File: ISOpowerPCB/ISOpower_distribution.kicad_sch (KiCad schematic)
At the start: 27 parts, among them M1 Fan_IEC60617, Q2 IRF5305_PBF, Q3 IRF5305_PBF, U10 LM2596S-5, U4 i6A4W020A-DC-DC-250W, U5 i6A4W020A-DC-DC-250W, U6 ACS712xLCTR-30A, U7 ACS712xLCTR-30A

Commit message: Footprint Associations 50% complete
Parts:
- C10, C20, C21, C9: footprint Capacitor_SMD:CP_Elec_10x10 -> Capacitor_SMD:CP_Elec_6.3x7.7
- C13, C14: footprint Capacitor_SMD:CP_Elec_6.3x5.9 -> Capacitor_SMD:CP_Elec_6.3x5.4
- C19: footprint Capacitor_SMD:CP_Elec_10x10 -> Capacitor_THT:C_Radial_D12.5mm_H20.0mm_P5.00mm
- D3: footprint Diode_THT:D_DO-201AD_P15.24mm_Horizontal -> Diode_SMD:D_SMA
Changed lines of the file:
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@@
     (property "Reference" "D3" (id 0) (at 247.65 140.97 90))
     (property "Value" "1N5821" (id 1) (at 246.38 144.78 90))
-    (property "Footprint" "Diode_THT:D_DO-201AD_P15.24mm_Horizontal" (id 2) (at 241.935 138.43 0)
+    (property "Footprint" "Diode_SMD:D_SMA" (id 2) (at 241.935 138.43 0)
       (effects (font (size 1.27 1.27)) hide)
     )
@@
       (effects (font (size 1.27 1.27)) (justify left))
     )
-    (property "Footprint" "Capacitor_SMD:CP_Elec_10x10" (id 2) (at 260.0452 142.24 0)
+    (property "Footprint" "Capacitor_SMD:CP_Elec_6.3x7.7" (id 2) (at 260.0452 142.24 0)
       (effects (font (size 1.27 1.27)) hide)
     )
@@
       (effects (font (size 1.27 1.27)) (justify left))
     )
-    (property "Footprint" "Capacitor_SMD:CP_Elec_10x10" (id 2) (at 206.7052 139.7 0)
+    (property "Footprint" "Capacitor_THT:C_Radial_D12.5mm_H20.0mm_P5.00mm" (id 2) (at 206.7052 139.7 0)
       (effects (font (size 1.27 1.27)) hide)
     )
@@
       (effects (font (size 1.27 1.27)) (justify left))
     )
-    (property "Footprint" "Capacitor_SMD:CP_Elec_6.3x5.9" (id 2) (at 122.8852 158.75 0)
+    (property "Footprint" "Capacitor_SMD:CP_Elec_6.3x5.4" (id 2) (at 122.8852 158.75 0)
       (effects (font (size 1.27 1.27)) hide)
     )
@@
       (effects (font (size 1.27 1.27)) (justify left))
     )
-    (property "Footprint" "Capacitor_SMD:CP_Elec_10x10" (id 2) (at 229.5652 63.5 0)
+    (property "Footprint" "Capacitor_SMD:CP_Elec_6.3x7.7" (id 2) (at 229.5652 63.5 0)
       (effects (font (size 1.27 1.27)) hide)
     )
@@
       (effects (font (size 1.27 1.27)) (justify left))
     )
-    (property "Footprint" "Capacitor_SMD:CP_Elec_10x10" (id 2) (at 41.6052 77.47 0)
+    (property "Footprint" "Capacitor_SMD:CP_Elec_6.3x7.7" (id 2) (at 41.6052 77.47 0)
       (effects (font (size 1.27 1.27)) hide)
     )
@@
       (effects (font (size 1.27 1.27)) (justify left))
     )
-    (property "Footprint" "Capacitor_SMD:CP_Elec_6.3x5.9" (id 2) (at 126.6952 80.01 0)
+    (property "Footprint" "Capacitor_SMD:CP_Elec_6.3x5.4" (id 2) (at 126.6952 80.01 0)
       (effects (font (size 1.27 1.27)) hide)
     )
@@
       (effects (font (size 1.27 1.27)) (justify left))
     )
-    (property "Footprint" "Capacitor_SMD:CP_Elec_10x10" (id 2) (at 42.8752 153.67 0)
-      (effects (font (size 1.27 1.27)) hide)
-    )
+    (property "Footprint" "Capacitor_SMD:CP_Elec_6.3x7.7" (id 2) (at 42.8752 153.67 0)
+      (effects (font (size 1.27 1.27)) hide)
+    )

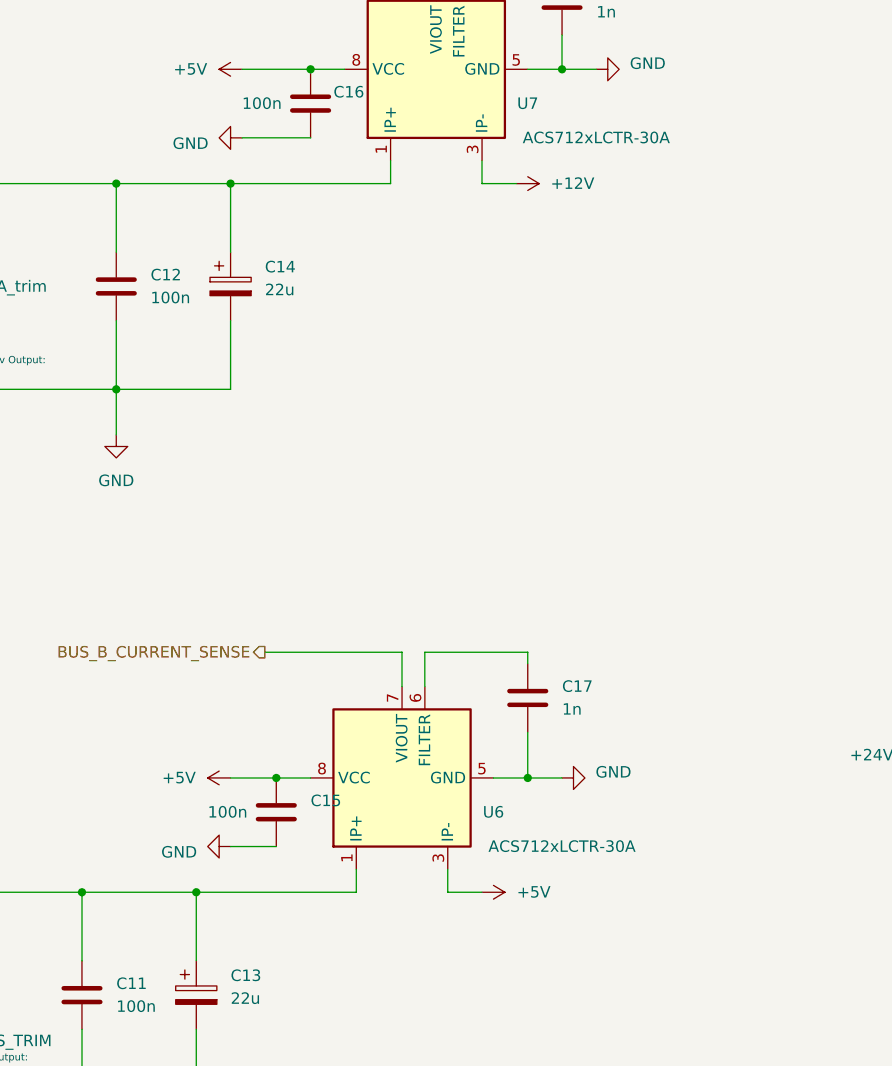
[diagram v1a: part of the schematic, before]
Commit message: added documentation for component selection
Completed footprint association & added documentation re Netclasses. Need to update netclasses in schematic settings before moving to PCB layout.
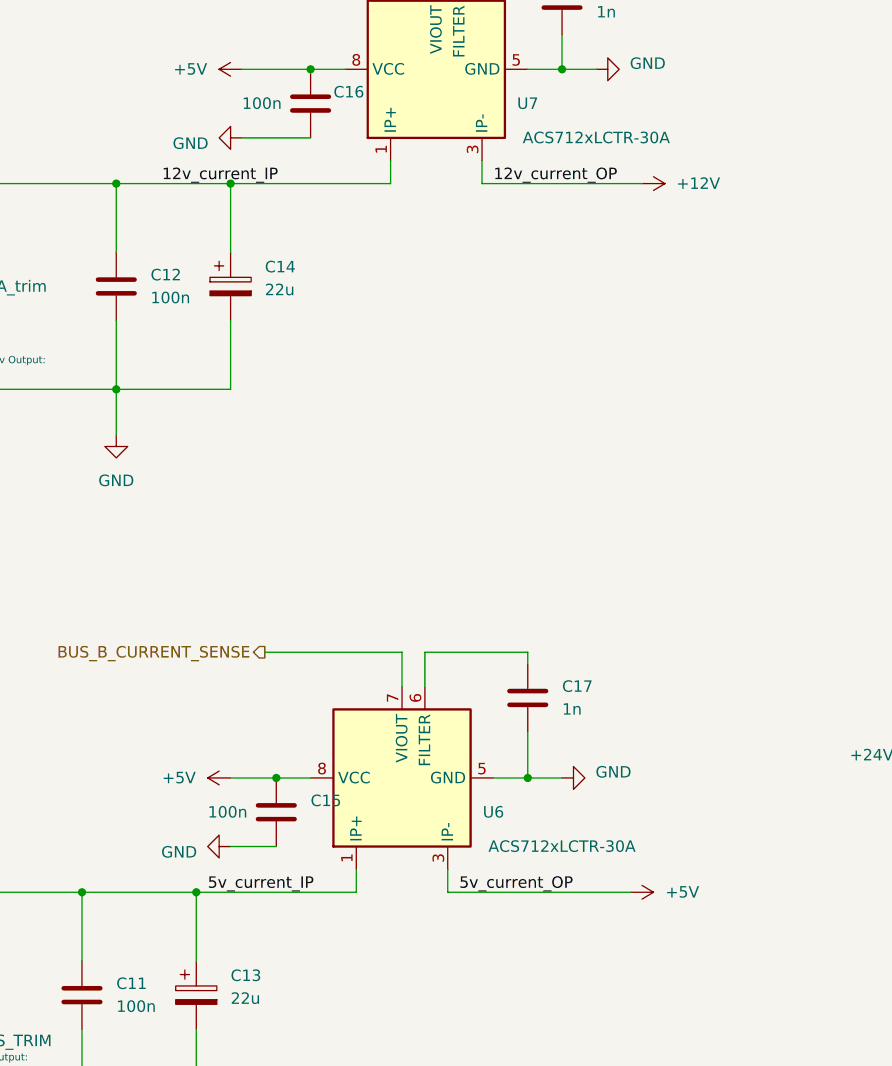
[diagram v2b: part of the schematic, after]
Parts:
- JP2, JP3: footprint (none) -> Jumper:SolderJumper-2_P1.3mm_Open_RoundedPad1.0x1.5mm
- L2: footprint (none) -> Inductor_SMD:L_12x12mm_H8mm
- M1: footprint Fuse:Fuseholder_Keystone_3555-2 -> ISOpower:Fan12V_40by10.5mm
- Q2, Q3: footprint Package_TO_SOT_THT:TO-220-3_Vertical -> Package_TO_SOT_SMD:TO-263-2
- R6, R7: footprint Resistor_SMD:R_0805_2012Metric_Pad1.20x1.40mm_HandSolder -> Resistor_THT:R_Axial_DIN0309_L9.0mm_D3.2mm_P12.70mm_Horizontal
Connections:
- net 5v_current_IP: now reaches C11.1, C13.1, U4.7 (Sense(+)), U4.8 (Vout(+)), U6.1 (IP+), U6.2 (IP+)
- net 12v_current_IP: now reaches C12.1, C14.1, U5.7 (Sense(+)), U5.8 (Vout(+)), U7.1 (IP+), U7.2 (IP+)
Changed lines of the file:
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@@
     (stroke (width 0) (type default) (color 0 0 0 0))
   )
-  (wire (pts (xy 149.86 143.51) (xy 153.67 143.51))
+  (wire (pts (xy 149.86 143.51) (xy 170.18 143.51))
     (stroke (width 0) (type default) (color 0 0 0 0))
   )
@@
     (stroke (width 0) (type default) (color 0 0 0 0))
   )
-  (wire (pts (xy 153.67 64.77) (xy 157.48 64.77))
+  (wire (pts (xy 153.67 64.77) (xy 171.45 64.77))
     (stroke (width 0) (type default) (color 0 0 0 0))
   )
@@
     (effects (font (size 1.27 1.27)) (justify left bottom))
   )
+  (label "12v_current_IP" (at 118.11 64.77 0)
+    (effects (font (size 1.27 1.27)) (justify left bottom))
+  )
+  (label "5v_current_OP" (at 151.13 143.51 0)
+    (effects (font (size 1.27 1.27)) (justify left bottom))
+  )
+  (label "12v_current_OP" (at 154.94 64.77 0)
+    (effects (font (size 1.27 1.27)) (justify left bottom))
+  )
   (label "12V_BUS" (at 29.21 30.48 0)
     (effects (font (size 1.27 1.27)) (justify left bottom))
@@
   )
   (label "MCU_5V" (at 260.35 133.35 0)
+    (effects (font (size 1.27 1.27)) (justify left bottom))
+  )
+  (label "5v_current_IP" (at 123.19 143.51 0)
     (effects (font (size 1.27 1.27)) (justify left bottom))
   )
@@
     (pin "1")
   )
-  (symbol (lib_id "power:+5V") (at 153.67 143.51 270) (unit 1)
-    (in_bom yes) (on_board yes)
-    (property "Reference" "#PWR043" (id 0) (at 149.86 143.51 0)
-      (effects (font (size 1.27 1.27)) hide)
-    )
-    (property "Value" "+5V" (id 1) (at 161.29 143.51 90)
+  (symbol (lib_id "power:+5V") (at 170.18 143.51 270) (unit 1)
+    (in_bom yes) (on_board yes)
+    (property "Reference" "#PWR043" (id 0) (at 166.37 143.51 0)
+      (effects (font (size 1.27 1.27)) hide)
+    )
+    (property "Value" "+5V" (id 1) (at 177.8 143.51 90)
       (effects (font (size 1.27 1.27)) (justify right))
     )
-    (property "Footprint" "" (id 2) (at 153.67 143.51 0)
-      (effects (font (size 1.27 1.27)) hide)
-    )
-    (property "Datasheet" "" (id 3) (at 153.67 143.51 0)
+    (property "Footprint" "" (id 2) (at 170.18 143.51 0)
+      (effects (font (size 1.27 1.27)) hide)
+    )
+    (property "Datasheet" "" (id 3) (at 170.18 143.51 0)
       (effects (font (size 1.27 1.27)) hide)
     )
@@
     (property "Reference" "L2" (id 0) (at 251.46 130.81 90))
     (property "Value" "33uH" (id 1) (at 252.73 134.62 90))
-    (property "Footprint" "" (id 2) (at 252.73 133.35 0)
+    (property "Footprint" "Inductor_SMD:L_12x12mm_H8mm" (id 2) (at 252.73 133.35 0)
       (effects (font (size 1.27 1.27)) hide)
     )
@@
       (effects (font (size 1.27 1.27)) (justify left))
     )
-    (property "Footprint" "Resistor_SMD:R_0805_2012Metric_Pad1.20x1.40mm_HandSolder" (id 2) (at 93.472 82.55 90)
+    (property "Footprint" "Resistor_THT:R_Axial_DIN0309_L9.0mm_D3.2mm_P12.70mm_Horizontal" (id 2) (at 93.472 82.55 90)
       (effects (font (size 1.27 1.27)) hide)
     )
@@
     (pin "2")
   )
-  (symbol (lib_id "power:+12V") (at 157.48 64.77 270) (unit 1)
-    (in_bom yes) (on_board yes) (fields_autoplaced)
-    (property "Reference" "#PWR044" (id 0) (at 153.67 64.77 0)
-      (effects (font (size 1.27 1.27)) hide)
-    )
-    (property "Value" "+12V" (id 1) (at 161.29 64.7699 90)
-      (effects (font (size 1.27 1.27)) (justify left))
-    )
-    (property "Footprint" "" (id 2) (at 157.48 64.77 0)
-      (effects (font (size 1.27 1.27)) hide)
-    )
-    (property "Datasheet" "" (id 3) (at 157.48 64.77 0)
+  (symbol (lib_id "power:+12V") (at 171.45 64.77 270) (unit 1)
+    (in_bom yes) (on_board yes) (fields_autoplaced)
+    (property "Reference" "#PWR044" (id 0) (at 167.64 64.77 0)
+      (effects (font (size 1.27 1.27)) hide)
+    )
+    (property "Value" "+12V" (id 1) (at 175.26 64.7699 90)
+      (effects (font (size 1.27 1.27)) (justify left))
+    )
+    (property "Footprint" "" (id 2) (at 171.45 64.77 0)
+      (effects (font (size 1.27 1.27)) hide)
+    )
+    (property "Datasheet" "" (id 3) (at 171.45 64.77 0)
       (effects (font (size 1.27 1.27)) hide)
     )
@@
     (property "Reference" "M1" (id 0) (at 219.71 62.23 90))
     (property "Value" "Fan_IEC60617" (id 1) (at 217.17 62.23 90))
-    (property "Footprint" "Fuse:Fuseholder_Keystone_3555-2" (id 2) (at 212.09 65.786 0)
+    (property "Footprint" "ISOpower:Fan12V_40by10.5mm" (id 2) (at 212.09 65.786 0)
       (effects (font (size 1.27 1.27)) (justify left) hide)
     )
@@
     (property "Reference" "JP3" (id 0) (at 50.8 86.36 90))
     (property "Value" "DSBL_BYPSS_A" (id 1) (at 52.07 90.17 90))
-    (property "Footprint" "" (id 2) (at 53.34 81.28 0)
+    (property "Footprint" "Jumper:SolderJumper-2_P1.3mm_Open_RoundedPad1.0x1.5mm" (id 2) (at 53.34 81.28 0)
       (effects (font (size 1.27 1.27)) hide)
     )
@@
     (property "Reference" "Q3" (id 0) (at 57.15 83.82 90))
     (property "Value" "IRF5305_PBF" (id 1) (at 66.04 81.28 90))
-    (property "Footprint" "Package_TO_SOT_THT:TO-220-3_Vertical" (id 2) (at 78.74 91.44 0)
+    (property "Footprint" "Package_TO_SOT_SMD:TO-263-2" (id 2) (at 78.74 91.44 0)
       (effects (font (size 1.27 1.27) italic) (justify left) hide)
     )
@@
     (property "Reference" "Q2" (id 0) (at 54.61 162.56 90))
     (property "Value" "IRF5305_PBF" (id 1) (at 63.5 160.02 90))
-    (property "Footprint" "Package_TO_SOT_THT:TO-220-3_Vertical" (id 2) (at 76.2 170.18 0)
+    (property "Footprint" "Package_TO_SOT_SMD:TO-263-2" (id 2) (at 76.2 170.18 0)
       (effects (font (size 1.27 1.27) italic) (justify left) hide)
     )
@@
     (property "Reference" "JP2" (id 0) (at 48.26 165.1 90))
     (property "Value" "DSBL_BYPSS_B" (id 1) (at 49.53 168.91 90))
-    (property "Footprint" "" (id 2) (at 50.8 160.02 0)
+    (property "Footprint" "Jumper:SolderJumper-2_P1.3mm_Open_RoundedPad1.0x1.5mm" (id 2) (at 50.8 160.02 0)
       (effects (font (size 1.27 1.27)) hide)
     )
@@
       (effects (font (size 1.27 1.27)) (justify left))
     )
-    (property "Footprint" "Resistor_SMD:R_0805_2012Metric_Pad1.20x1.40mm_HandSolder" (id 2) (at 89.662 161.29 90)
-      (effects (font (size 1.27 1.27)) hide)
-    )
+    (property "Footprint" "Resistor_THT:R_Axial_DIN0309_L9.0mm_D3.2mm_P12.70mm_Horizontal" (id 2) (at 89.662 161.29 90)
+      (effects (font (size 1.27 1.27)) hide)
+    )
